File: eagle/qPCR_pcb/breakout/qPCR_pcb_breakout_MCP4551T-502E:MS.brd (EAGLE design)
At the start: 17.8 x 22.9 mm, 3 parts, among them U1 MCP4551T-502E/MS

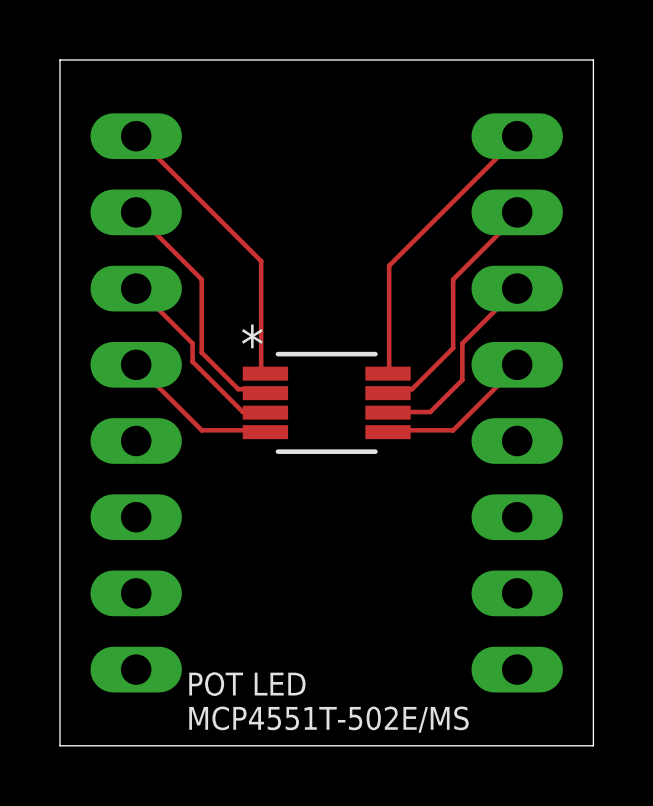
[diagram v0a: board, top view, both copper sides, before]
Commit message: add female headers
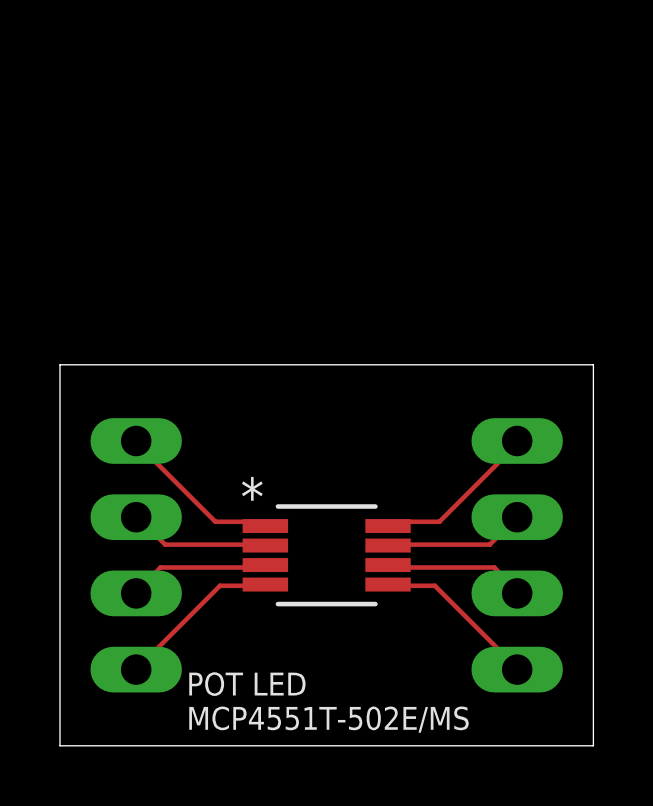
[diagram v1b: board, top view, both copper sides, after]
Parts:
- removed JP2: (no value), pinhead:1X08
- added JP3: (no value), pinhead:1X04
- JP1: device pinhead:1X08 -> pinhead:1X04
- moved JP1 5.08 mm to (2.54, 6.35)
- moved U1 5.08 mm to (8.89, 6.35)
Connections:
- removed net 10: JP2.7
- removed net 11: JP2.6
- removed net 12: JP2.5
- removed net 13: JP2.4, U1.5
- removed net 14: JP2.3, U1.6
- removed net 15: JP2.2, U1.7
- removed net 16: JP2.1, U1.8
- removed net 9: JP2.8
- net 5: now also JP3.4, U1.5; no longer JP1.5
- net 6: now also JP3.3, U1.6; no longer JP1.6
- net 7: now also JP3.2, U1.7; no longer JP1.7
- net 8: now also JP3.1, U1.8; no longer JP1.8
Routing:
- net 16: track 9.69 -> 0.00 mm
- net 15: track 8.24 -> 0.00 mm
- net 14: track 6.73 -> 0.00 mm
- net 8: track 0.00 -> 5.59 mm
- net 5: track 0.00 -> 5.51 mm
- net 13: track 5.27 -> 0.00 mm
- net 6: track 0.00 -> 4.77 mm
- net 7: track 0.00 -> 4.70 mm
- net 1: track 9.72 -> 5.50 mm
- net 2: track 8.25 -> 4.69 mm
- net 3: track 6.37 -> 4.71 mm
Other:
- board size 17.8 x 22.9 mm -> 17.8 x 12.7 mm
